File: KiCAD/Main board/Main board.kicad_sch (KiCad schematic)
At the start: 20 parts, among them J1 Conn_01x03, J10 Conn_01x03, J11 Conn_01x03, J12 Conn_01x03, J2 Conn_01x03, J3 Conn_01x02, J4 Conn_01x02, J5 Conn_01x03, J6 Conn_01x02, J7 Conn_01x03, J8 Conn_01x02, J9 Conn_01x03

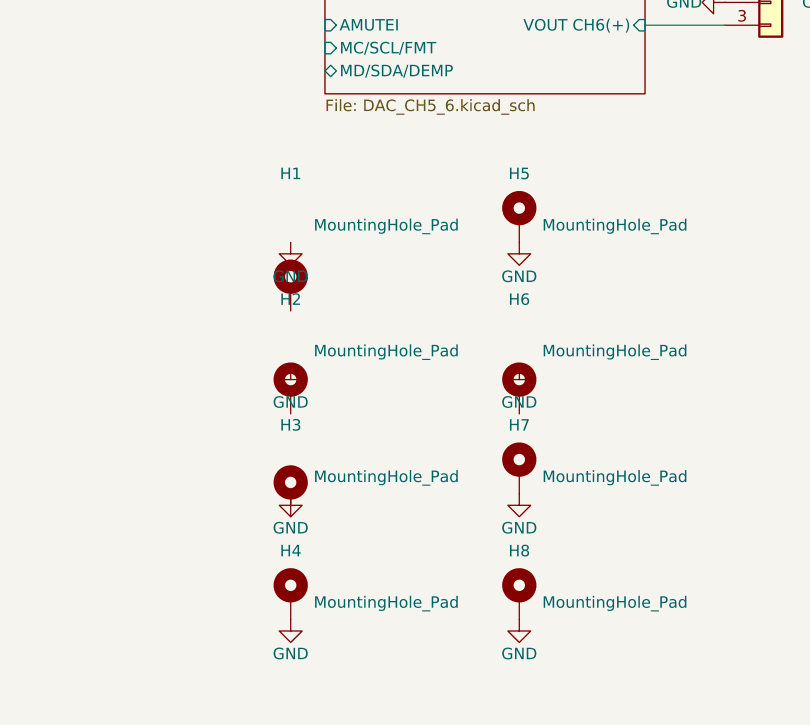
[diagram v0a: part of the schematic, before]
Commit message: Added SEPIC symbol and footprint and worked on main board
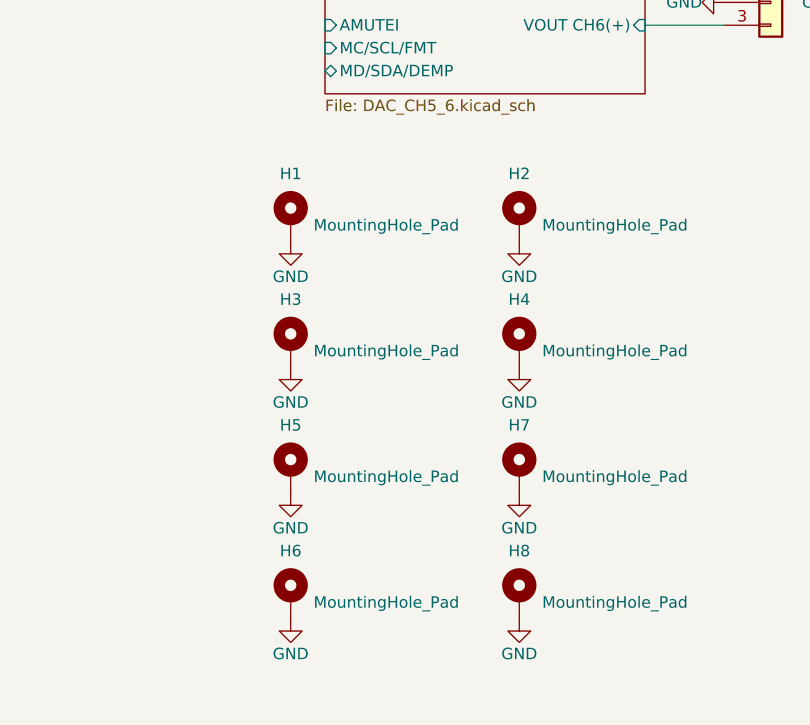
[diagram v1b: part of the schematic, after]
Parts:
- H3: footprint MountingHole:MountingHole_3.5mm_Pad_Via -> (none)
- H5, H7: now left out of the parts list
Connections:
- net GND: now also H1.1, H2.1, H3.1, H6.1

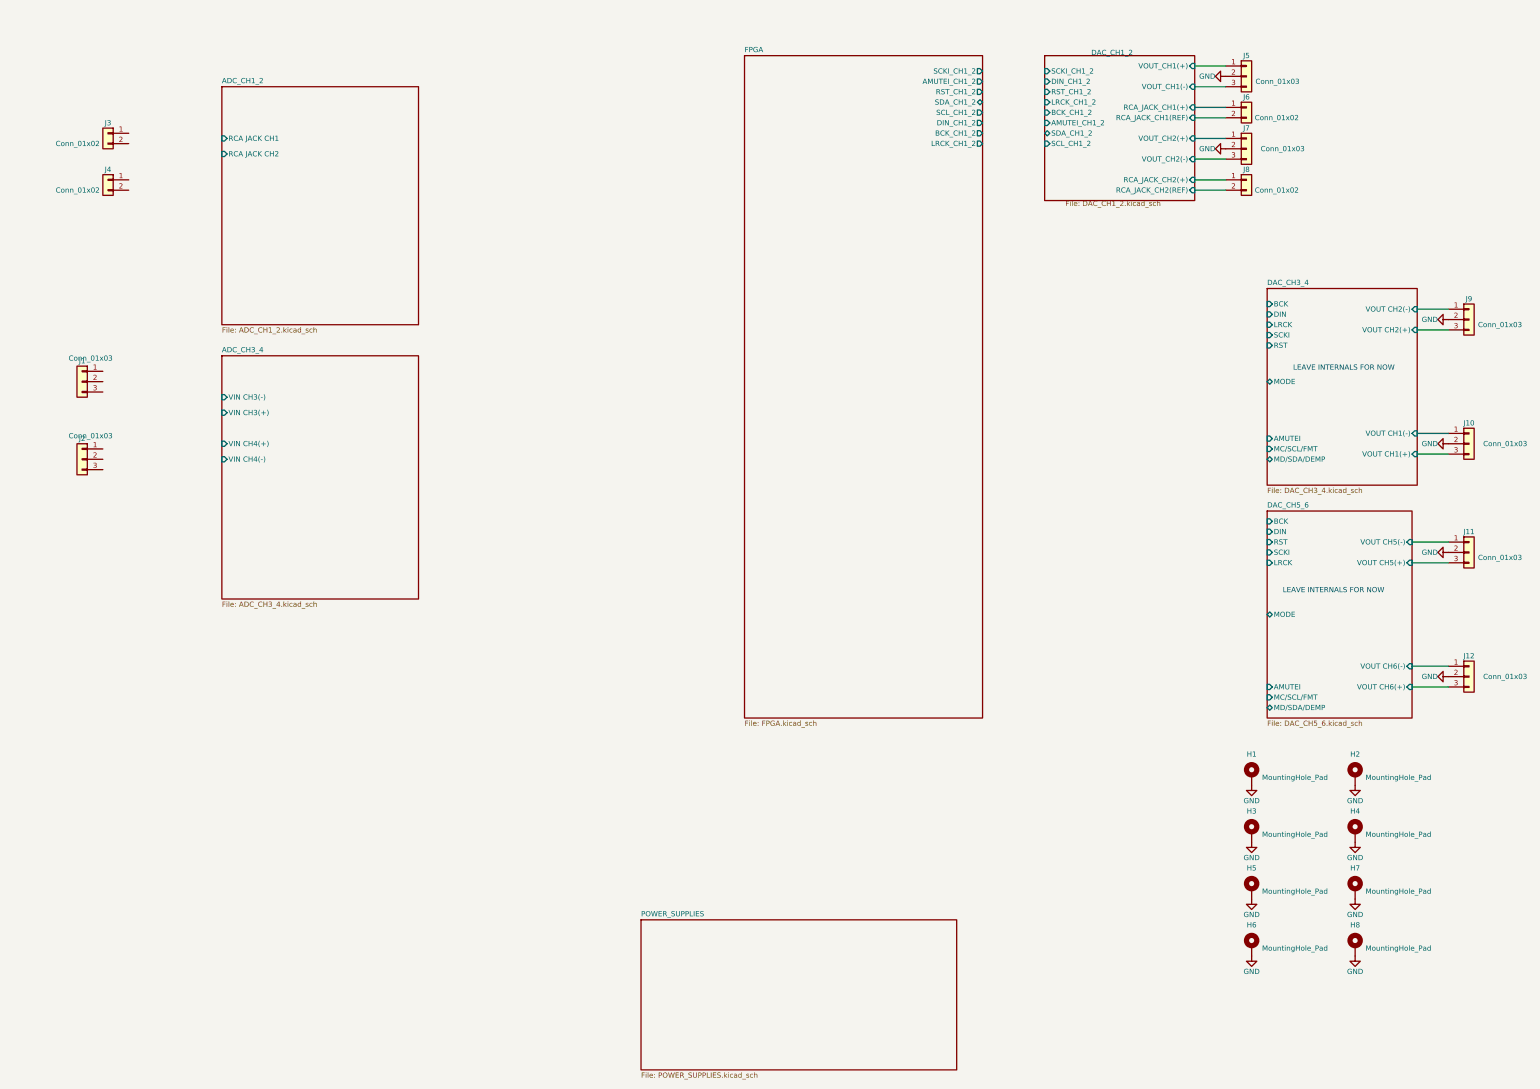
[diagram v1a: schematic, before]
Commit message: Worked on main board schematic and PCB, added symbols to symbol library
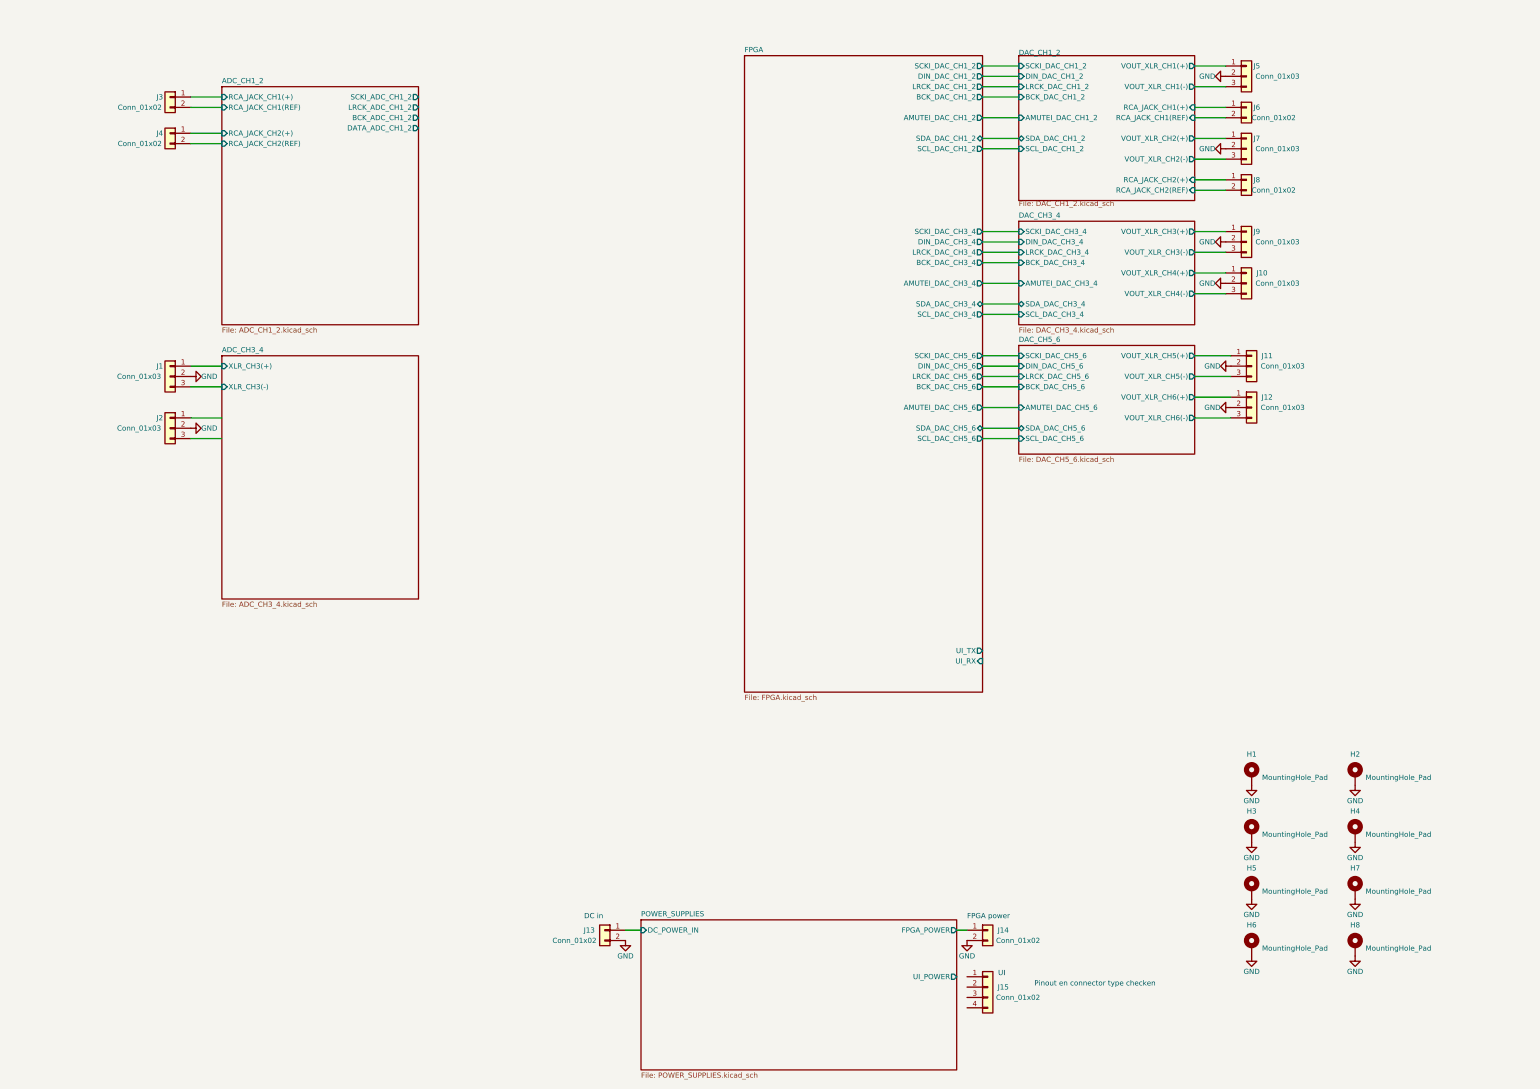
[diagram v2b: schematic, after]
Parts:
- added J13, J14: Conn_01x02, Connector_Phoenix_MC:PhoenixContact_MCV_1,5_2-G-3.5_1x02_P3.50mm_Vertical, symbol Connector_Generic:Conn_01x02
- added J15: Conn_01x02, Connector_Phoenix_MC:PhoenixContact_MCV_1,5_2-G-3.5_1x02_P3.50mm_Vertical, symbol Connector_Generic:Conn_01x04
- H1, H2, H3, H4, H5, H6, H7, H8: footprint (none) -> MountingHole:MountingHole_3.5mm_Pad_Via
- J1, J10, J11, J12, J2, J5, J7, J9: footprint (none) -> Connector_JST:JST_PH_B3B-PH-K_1x03_P2.00mm_Vertical
- J3, J4, J6, J8: footprint (none) -> Connector_JST:JST_PH_B2B-PH-K_1x02_P2.00mm_Vertical
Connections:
- net GND: now also J1.2 (Pin_2), J2.2 (Pin_2), J13.2 (Pin_2), J14.2 (Pin_2)
- net ADC_CH3_4/XLR_CH3(+): now reaches J1.1 (Pin_1)
- net ADC_CH3_4/XLR_CH3(-): now reaches J1.3 (Pin_3)
- net ADC_CH1_2/RCA_JACK_CH1(+): now reaches J3.1 (Pin_1)
- net ADC_CH1_2/RCA_JACK_CH1(REF): now reaches J3.2 (Pin_2)
- net ADC_CH1_2/RCA_JACK_CH2(+): now reaches J4.1 (Pin_1)
- net ADC_CH1_2/RCA_JACK_CH2(REF): now reaches J4.2 (Pin_2)
- net DAC_CH1_2/VOUT_CH1(+) renamed DAC_CH1_2/VOUT_XLR_CH1(+)
- net DAC_CH1_2/VOUT_CH1(-) renamed DAC_CH1_2/VOUT_XLR_CH1(-)
- net DAC_CH1_2/VOUT_CH2(+) renamed DAC_CH1_2/VOUT_XLR_CH2(+)
- net DAC_CH1_2/VOUT_CH2(-) renamed DAC_CH1_2/VOUT_XLR_CH2(-)
- net DAC_CH3_4/VOUT CH1(+) renamed DAC_CH3_4/VOUT_XLR_CH4(-)
- net DAC_CH3_4/VOUT CH1(-) renamed DAC_CH3_4/VOUT_XLR_CH4(+)
- net DAC_CH3_4/VOUT CH2(+) renamed DAC_CH3_4/VOUT_XLR_CH3(-)
- net DAC_CH3_4/VOUT CH2(-) renamed DAC_CH3_4/VOUT_XLR_CH3(+)
- net DAC_CH5_6/VOUT CH5(+) renamed DAC_CH5_6/VOUT_XLR_CH5(-)
- net DAC_CH5_6/VOUT CH5(-) renamed DAC_CH5_6/VOUT_XLR_CH5(+)
- net DAC_CH5_6/VOUT CH6(+) renamed DAC_CH5_6/VOUT_XLR_CH6(-)
- net DAC_CH5_6/VOUT CH6(-) renamed DAC_CH5_6/VOUT_XLR_CH6(+)
- new net POWER_SUPPLIES/DC_POWER_IN: J13.1 (Pin_1)
- new net POWER_SUPPLIES/FPGA_POWER: J14.1 (Pin_1)
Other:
- sheet ADC_CH1_2 ports: added BCK_ADC_CH1_2, DATA_ADC_CH1_2, LRCK_ADC_CH1_2, RCA_JACK_CH1(+), RCA_JACK_CH1(REF), RCA_JACK_CH2(+), RCA_JACK_CH2(REF), SCKI_ADC_CH1_2; removed RCA JACK CH1, RCA JACK CH2
- sheet ADC_CH3_4 ports: added XLR_CH3(+), XLR_CH3(-); removed VIN CH3(+), VIN CH3(-), VIN CH4(+), VIN CH4(-)
- sheet DAC_CH1_2 ports: added AMUTEI_DAC_CH1_2, BCK_DAC_CH1_2, DIN_DAC_CH1_2, LRCK_DAC_CH1_2, SCKI_DAC_CH1_2, SCL_DAC_CH1_2, SDA_DAC_CH1_2, VOUT_XLR_CH1(+), VOUT_XLR_CH1(-), VOUT_XLR_CH2(+), VOUT_XLR_CH2(-); removed AMUTEI_CH1_2, BCK_CH1_2, DIN_CH1_2, LRCK_CH1_2, RST_CH1_2, SCKI_CH1_2, SCL_CH1_2, SDA_CH1_2, VOUT_CH1(+), VOUT_CH1(-), VOUT_CH2(+), VOUT_CH2(-)
- sheet DAC_CH3_4 ports: added AMUTEI_DAC_CH3_4, BCK_DAC_CH3_4, DIN_DAC_CH3_4, LRCK_DAC_CH3_4, SCKI_DAC_CH3_4, SCL_DAC_CH3_4, SDA_DAC_CH3_4, VOUT_XLR_CH3(+), VOUT_XLR_CH3(-), VOUT_XLR_CH4(+), VOUT_XLR_CH4(-); removed AMUTEI, BCK, DIN, LRCK, MC/SCL/FMT, MD/SDA/DEMP, MODE, RST, SCKI, VOUT CH1(+), VOUT CH1(-), VOUT CH2(+), VOUT CH2(-)
- sheet DAC_CH5_6 ports: added AMUTEI_DAC_CH5_6, BCK_DAC_CH5_6, DIN_DAC_CH5_6, LRCK_DAC_CH5_6, SCKI_DAC_CH5_6, SCL_DAC_CH5_6, SDA_DAC_CH5_6, VOUT_XLR_CH5(+), VOUT_XLR_CH5(-), VOUT_XLR_CH6(+), VOUT_XLR_CH6(-); removed AMUTEI, BCK, DIN, LRCK, MC/SCL/FMT, MD/SDA/DEMP, MODE, RST, SCKI, VOUT CH5(+), VOUT CH5(-), VOUT CH6(+), VOUT CH6(-)
- sheet FPGA ports: added AMUTEI_DAC_CH1_2, AMUTEI_DAC_CH3_4, AMUTEI_DAC_CH5_6, BCK_DAC_CH1_2, BCK_DAC_CH3_4, BCK_DAC_CH5_6, DIN_DAC_CH1_2, DIN_DAC_CH3_4, DIN_DAC_CH5_6, LRCK_DAC_CH1_2, LRCK_DAC_CH3_4, LRCK_DAC_CH5_6, SCKI_DAC_CH1_2, SCKI_DAC_CH3_4, SCKI_DAC_CH5_6, SCL_DAC_CH1_2, SCL_DAC_CH3_4, SCL_DAC_CH5_6, SDA_DAC_CH1_2, SDA_DAC_CH3_4, SDA_DAC_CH5_6, UI_RX, UI_TX; removed AMUTEI_CH1_2, BCK_CH1_2, DIN_CH1_2, LRCK_CH1_2, RST_CH1_2, SCKI_CH1_2, SCL_CH1_2, SDA_CH1_2
- sheet POWER_SUPPLIES ports: added DC_POWER_IN, FPGA_POWER, UI_POWER; removed none
- note added: "DC in"
- note added: "FPGA power"
- note added: "Pinout en connector type checken"
- note added: "UI"
- note removed: "LEAVE INTERNALS FOR NOW"
- moved on the sheet: J1, J10, J11, J12, J2, J3, J4, J9

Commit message: Worked on main board design
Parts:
- added J16, J17: Conn_01x02, Connector_JST:JST_PH_B2B-PH-K_1x02_P2.00mm_Vertical, symbol Connector_Generic:Conn_01x02
- J15: value Conn_01x02 -> Conn_01x04; footprint Connector_Phoenix_MC:PhoenixContact_MCV_1,5_2-G-3.5_1x02_P3.50mm_Vertical -> Connector_PinHeader_2.54mm:PinHeader_1x04_P2.54mm_Vertical
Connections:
- net ADC_CH3_4/XLR_CH4(+): now reaches J2.1 (Pin_1)
- net ADC_CH3_4/XLR_CH4(-): now reaches J2.3 (Pin_3)
- net ADC_CH1_2/RCA_JACK_CH1(+) renamed ADC_CH1_2/RCA_CH1(+)
- net ADC_CH1_2/RCA_JACK_CH1(REF) renamed ADC_CH1_2/RCA_CH1(REF)
- net ADC_CH1_2/RCA_JACK_CH2(+) renamed ADC_CH1_2/JACK_CH1(+)
- net ADC_CH1_2/RCA_JACK_CH2(REF) renamed ADC_CH1_2/JACK_CH1(REF)
- new net ADC_CH1_2/JACK_CH2(+): J17.1 (Pin_1)
- new net ADC_CH1_2/JACK_CH2(REF): J17.2 (Pin_2)
- new net ADC_CH1_2/RCA_CH2(+): J16.1 (Pin_1)
- new net ADC_CH1_2/RCA_CH2(REF): J16.2 (Pin_2)
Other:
- sheet ADC_CH1_2 ports: added INPUT_SELECTOR_RELAY_CH1, INPUT_SELECTOR_RELAY_CH2, JACK_CH1(+), JACK_CH1(REF), JACK_CH2(+), JACK_CH2(REF), RCA_CH1(+), RCA_CH1(REF), RCA_CH2(+), RCA_CH2(REF); removed RCA_JACK_CH1(+), RCA_JACK_CH1(REF), RCA_JACK_CH2(+), RCA_JACK_CH2(REF)
- sheet ADC_CH3_4 ports: added XLR_CH4(+), XLR_CH4(-); removed none
- sheet FPGA ports: added BCK_ADC_CH1_2, DATA_ADC_CH1_2, INPUT_SELECTOR_RELAY_CH1, INPUT_SELECTOR_RELAY_CH2, LRCK_ADC_CH1_2, SCKI_ADC_CH1_2; removed none
- sheet POWER_SUPPLIES ports: added none; removed UI_POWER
- note added: "Pinout checken en kabel lengte"
- note removed: "Pinout en connector type checken"
- moved on the sheet: J1, J15, J2, J3, J4

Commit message: Worked on main board
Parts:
- added J18 (x4): Conn_01x05, Connector_JST:JST_XH_B5B-XH-A_1x05_P2.50mm_Vertical, symbol Connector_Generic:Conn_01x05
- J15: value Conn_01x04 -> Conn_01x06; footprint Connector_PinHeader_2.54mm:PinHeader_1x04_P2.54mm_Vertical -> Connector_JST:JST_PH_B6B-PH-K_1x06_P2.00mm_Vertical; symbol Connector_Generic:Conn_01x04 -> Connector_Generic:Conn_01x06; Datasheet cable (none) -> https://www.tinytronics.nl/shop/nl/kabels-en-connectoren/ka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
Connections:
- net +5VD1: now also J15.3 (Pin_3), J18.1 (Pin_1), J18.1 (Pin_1), J18.1 (Pin_1), J18.1 (Pin_1)
- net FPGA/UI_RX: now also J15.6 (Pin_6)
- net FPGA/UI_TX: now also J15.4 (Pin_4)
- net GND: now also J15.1 (Pin_1)
- new net ADC_CH1_2/VU_LED1_CH1: J18.2 (Pin_2)
- new net ADC_CH1_2/VU_LED1_CH2: J18.2 (Pin_2)
- new net ADC_CH1_2/VU_LED2_CH1: J18.3 (Pin_3)
- new net ADC_CH1_2/VU_LED2_CH2: J18.3 (Pin_3)
- new net ADC_CH1_2/VU_LED3_CH1: J18.4 (Pin_4)
- new net ADC_CH1_2/VU_LED3_CH2: J18.4 (Pin_4)
- new net ADC_CH1_2/VU_LED4_CH1: J18.5 (Pin_5)
- new net ADC_CH1_2/VU_LED4_CH2: J18.5 (Pin_5)
- no-connect marks 0 -> 2
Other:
- sheet ADC_CH1_2 ports: added VU_LED1_CH1, VU_LED1_CH2, VU_LED2_CH1, VU_LED2_CH2, VU_LED3_CH1, VU_LED3_CH2, VU_LED4_CH1, VU_LED4_CH2; removed none
- note added: "Pinout checken"
- note added: "Power lines are not routed in this view to keep this page more clear"
- note removed: "Pinout checken en kabel lengte"
- moved on the sheet: J1, J16, J17, J2, J3, J4

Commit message: Worked on main board
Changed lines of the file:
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@@
     )
   )
-  (sheet (at 193.04 25.4) (size 58.42 156.21) (fields_autoplaced)
+  (sheet (at 193.04 25.4) (size 58.42 120.65) (fields_autoplaced)
     (stroke (width 0.1524) (type solid))
     (fill (color 0 0 0 0.0000))
@@
       (effects (font (size 1.27 1.27)) (justify left bottom))
     )
-    (property "Sheetfile" "FPGA.kicad_sch" (at 193.04 182.1946 0)
+    (property "Sheetfile" "FPGA.kicad_sch" (at 193.04 146.6346 0)
       (effects (font (size 1.27 1.27)) (justify left top))
     )

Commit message: Worked in main board
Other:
- sheet ADC_CH1_2 ports: added TXS0102_SCLK_CH1_2, TXS0102_SDA_CH1_2, ~{RST_ADC_CH1_2}, ~{TXS0102_OE_CH1_2}; removed none
- sheet FPGA ports: added TXS0102_SCLK_CH1_2, TXS0102_SDA_CH1_2, ~{RST_ADC_CH1_2}, ~{TXS0102_OE_CH1_2}; removed none
- note added: "Just a note"
- note added: "Point of attention"
- note removed: "Pinout checken"
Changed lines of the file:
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@@
   (no_connect (at 312.42 133.35))
   (no_connect (at 312.42 140.97))
-  (wire (pts (xy 184.15 43.18) (xy 193.04 43.18))
+  (wire (pts (xy 184.15 48.26) (xy 193.04 48.26))
     (stroke (width 0) (type default))
   )
@@
     (stroke (width 0) (type default))
   )
+  (wire (pts (xy 184.15 53.34) (xy 193.04 53.34))
+    (stroke (width 0) (type default))
+  )
   (wire (pts (xy 303.53 99.06) (xy 312.42 99.06))
     (stroke (width 0) (type default))
@@
     (stroke (width 0) (type default))
   )
+  (wire (pts (xy 184.15 55.88) (xy 193.04 55.88))
+    (stroke (width 0) (type default))
+  )
   (wire (pts (xy 251.46 73.66) (xy 260.35 73.66))
     (stroke (width 0) (type default))
@@
     (stroke (width 0) (type default))
   )
+  (wire (pts (xy 184.15 58.42) (xy 193.04 58.42))
+    (stroke (width 0) (type default))
+  )
   (wire (pts (xy 303.53 73.66) (xy 311.15 73.66))
     (stroke (width 0) (type default))
@@
     (stroke (width 0) (type default))
   )
+  (wire (pts (xy 184.15 40.64) (xy 193.04 40.64))
+    (stroke (width 0) (type default))
+  )
   (wire (pts (xy 303.53 68.58) (xy 311.15 68.58))
     (stroke (width 0) (type default))
@@
     (stroke (width 0) (type default))
   )
-  (wire (pts (xy 184.15 40.64) (xy 193.04 40.64))
+  (wire (pts (xy 184.15 45.72) (xy 193.04 45.72))
     (stroke (width 0) (type default))
   )
@@
   (wire (pts (xy 251.46 45.72) (xy 260.35 45.72))
     (stroke (width 0) (type default))
+  )
+  (text "Just a note" (at 300.99 257.81 0)
+    (effects (font (size 1.27 1.27)) (justify left bottom))
   )
   (text "FPGA power" (at 247.65 237.49 0)
@@
     (effects (font (size 1.27 1.27)) (justify left bottom))
   )
-  (text "Pinout checken" (at 307.34 147.32 0)
-    (effects (font (size 1.27 1.27) (color 200 0 200 1)) (justify left bottom))
-  )
   (text "DC in" (at 153.67 237.49 0)
     (effects (font (size 1.27 1.27)) (justify left bottom))
+  )
+  (text "Point of attention" (at 300.99 255.27 0)
+    (effects (font (size 1.27 1.27) (color 200 0 200 1)) (justify left bottom))
   )
   (text "Power lines are not routed in this view to keep this page more clear"
@@
       (effects (font (size 1.27 1.27)) (justify right))
     )
-    (pin "INPUT_SELECTOR_RELAY_CH1" output (at 193.04 40.64 180)
-      (effects (font (size 1.27 1.27)) (justify left))
-    )
-    (pin "INPUT_SELECTOR_RELAY_CH2" output (at 193.04 43.18 180)
+    (pin "INPUT_SELECTOR_RELAY_CH1" output (at 193.04 45.72 180)
+      (effects (font (size 1.27 1.27)) (justify left))
+    )
+    (pin "INPUT_SELECTOR_RELAY_CH2" output (at 193.04 48.26 180)
       (effects (font (size 1.27 1.27)) (justify left))
     )
@@
     )
     (pin "DATA_ADC_CH1_2" input (at 193.04 35.56 180)
+      (effects (font (size 1.27 1.27)) (justify left))
+    )
+    (pin "~{TXS0102_OE_CH1_2}" output (at 193.04 58.42 180)
+      (effects (font (size 1.27 1.27)) (justify left))
+    )
+    (pin "TXS0102_SDA_CH1_2" bidirectional (at 193.04 55.88 180)
+      (effects (font (size 1.27 1.27)) (justify left))
+    )
+    (pin "TXS0102_SCLK_CH1_2" output (at 193.04 53.34 180)
+      (effects (font (size 1.27 1.27)) (justify left))
+    )
+    (pin "~{RST_ADC_CH1_2}" output (at 193.04 40.64 180)
       (effects (font (size 1.27 1.27)) (justify left))
     )
@@
       (effects (font (size 1.27 1.27)) (justify right))
     )
-    (pin "INPUT_SELECTOR_RELAY_CH1" input (at 184.15 40.64 0)
-      (effects (font (size 1.27 1.27)) (justify right))
-    )
-    (pin "INPUT_SELECTOR_RELAY_CH2" input (at 184.15 43.18 0)
+    (pin "INPUT_SELECTOR_RELAY_CH1" input (at 184.15 45.72 0)
+      (effects (font (size 1.27 1.27)) (justify right))
+    )
+    (pin "INPUT_SELECTOR_RELAY_CH2" input (at 184.15 48.26 0)
       (effects (font (size 1.27 1.27)) (justify right))
     )
@@
       (effects (font (size 1.27 1.27)) (justify left))
     )
-    (instances
+    (pin "TXS0102_SDA_CH1_2" bidirectional (at 184.15 55.88 0)
+      (effects (font (size 1.27 1.27)) (justify right))
+    )
+    (pin "TXS0102_SCLK_CH1_2" input (at 184.15 53.34 0)
+      (effects (font (size 1.27 1.27)) (justify right))
+    )
+    (pin "~{TXS0102_OE_CH1_2}" input (at 184.15 58.42 0)
+      (effects (font (size 1.27 1.27)) (justify right))
+    )
+    (pin "~{RST_ADC_CH1_2}" input (at 184.15 40.64 0)
+      (effects (font (size 1.27 1.27)) (justify right))
+    )
+    (instances
